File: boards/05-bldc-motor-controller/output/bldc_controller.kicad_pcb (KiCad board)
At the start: 2 copper layers, 80 x 100 mm, 55 parts, among them J1 Power Input, J2 Motor Output, J3 Hall Sensors, J4 SWD-6, Q1 IRLZ44N, Q2 IRLZ44N, Q3 IRLZ44N, Q4 IRLZ44N, Q5 IRLZ44N, Q6 IRLZ44N, U1 LM2596-5.0, U10 STM32G431K8Tx, U2 AMS1117-3.3, U3 DRV8301, Y1 8MHz

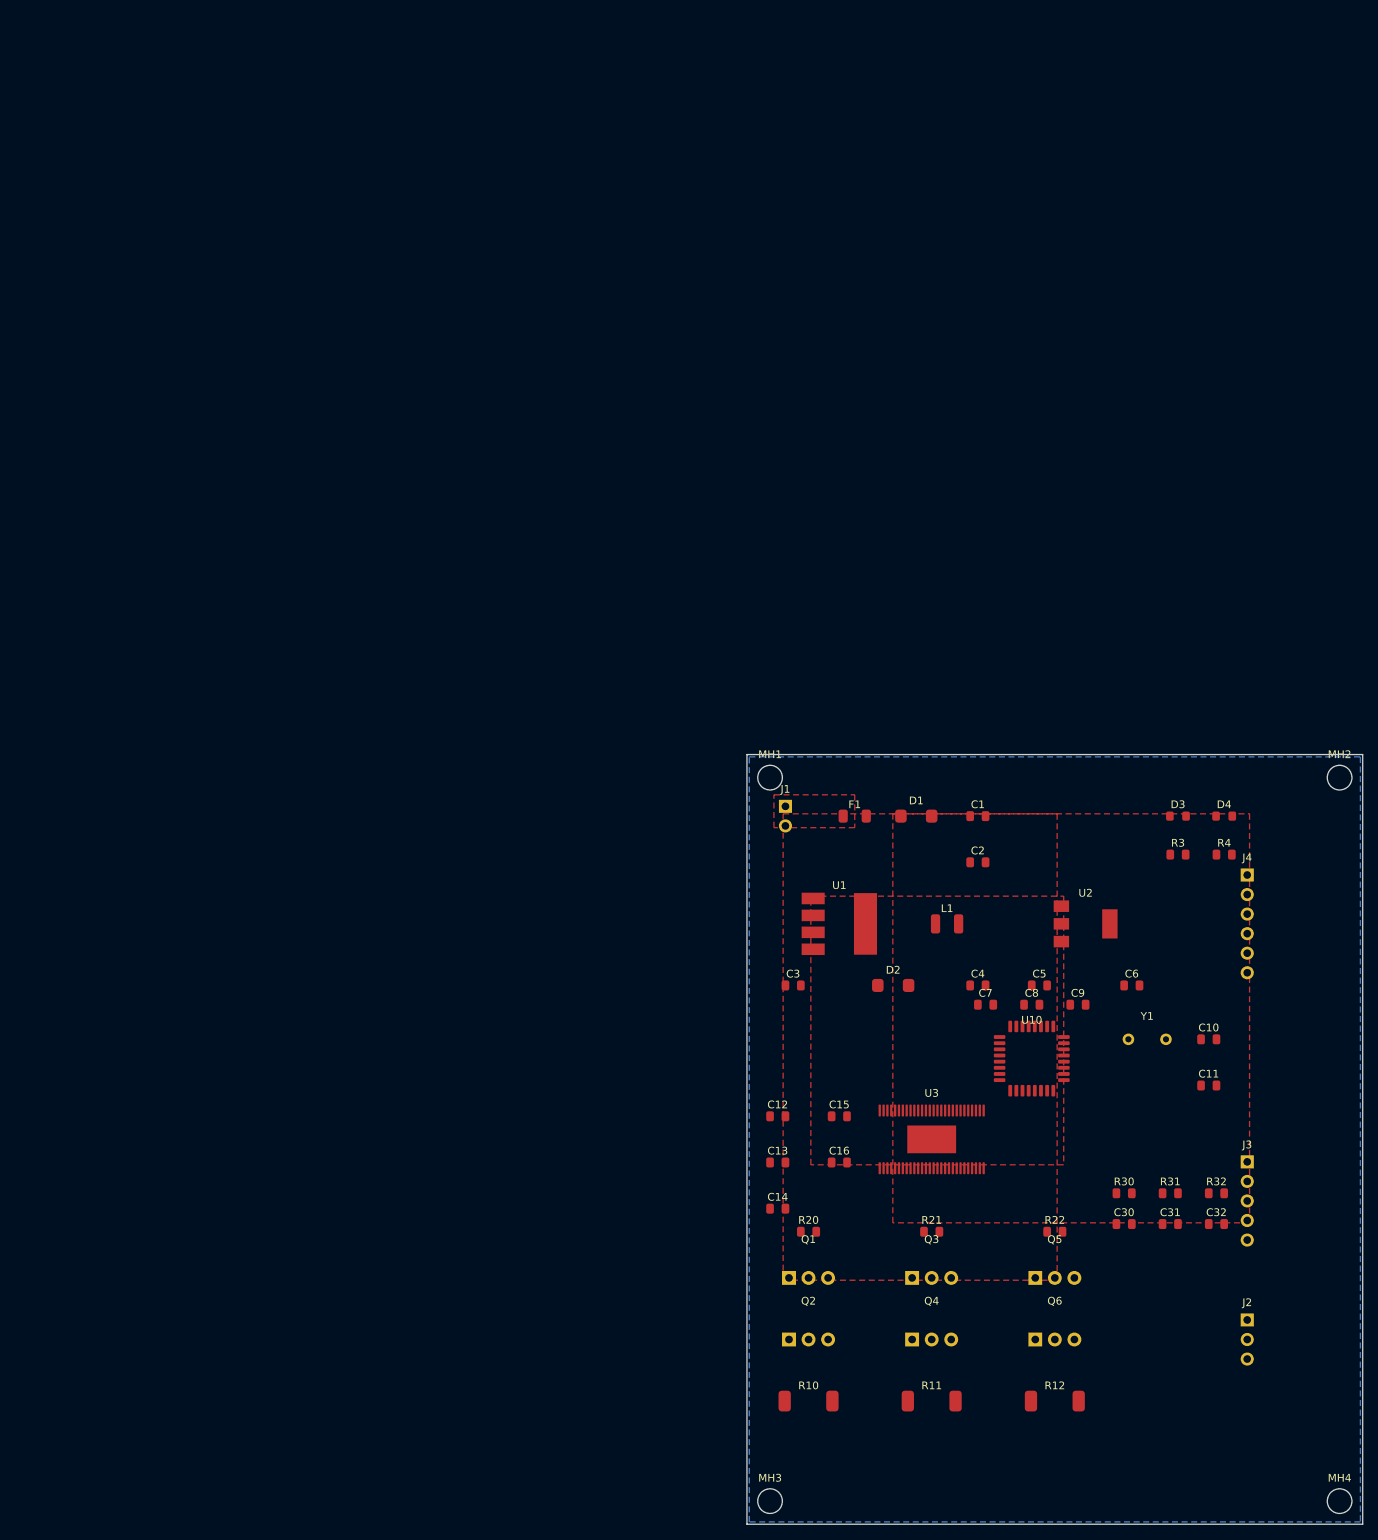
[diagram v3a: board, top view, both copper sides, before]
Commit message: feat(pcb): add page_fit to size sheet to board + center, apply to all boards
Add PCB.page_fit(margin=5.0) which rewrites the (paper ...) node to a tight
(paper "User" W H) sized to the Edge.Cuts bbox plus a uniform margin and
translates every board item (footprints, segments, vias, zones incl.
filled_polygons, gr_* graphics, text) so the board is centered with that
margin. Pure geometric translate — relative geometry, routing and DRC
validity are preserved, no re-route needed.

Expose it as `kct pcb page-fit <pcb> [-o out] [--margin] [--dry-run]` and
wire a PAGE_FIT build step (after stitch, before verify/export) so future
boards are centered too. Apply page_fit to all demo boards (00-07 +
external/softstart), both routed and unrouted PCBs, so the committed
layouts fill + center the KiCanvas viewer instead of sitting tiny in an A4
page. Boards 00/01 stay DRC-clean (0 errors); no board's DRC count changed.

Co-Authored-By: Claude Opus 4.7 <noreply@anthropic.com>
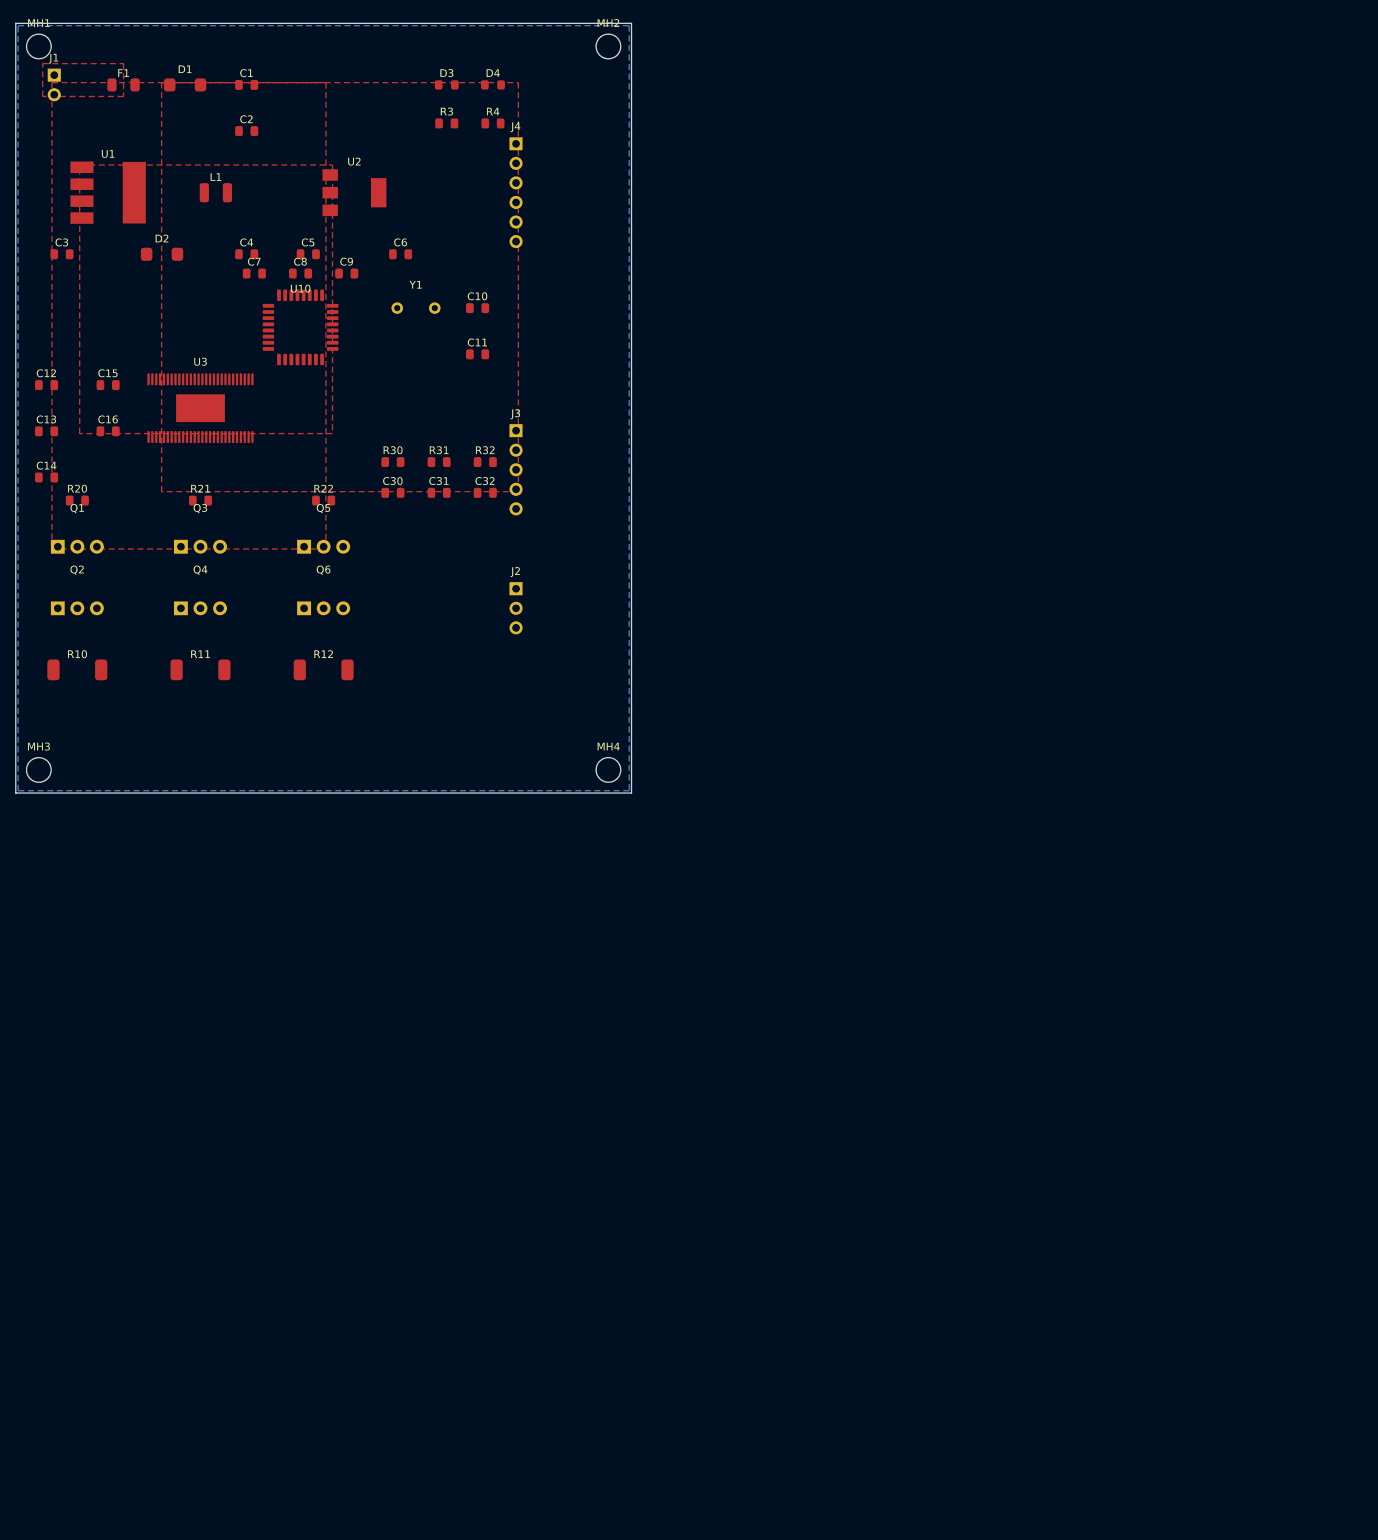
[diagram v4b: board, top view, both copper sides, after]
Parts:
- moved C1 134.4 mm to (35.0, 13.0)
- moved C10 134.4 mm to (65.0, 42.0)
- moved C11 134.4 mm to (65.0, 48.0)
- moved C12 134.4 mm to (9.00, 52.0)
- moved C13 134.4 mm to (9.00, 58.0)
- moved C14 134.4 mm to (9.00, 64.0)
- moved C15 134.4 mm to (17.0, 52.0)
- moved C16 134.4 mm to (17.0, 58.0)
- moved C2 134.4 mm to (35.0, 19.0)
- moved C3 134.4 mm to (11.0, 35.0)
- moved C30 134.4 mm to (54.0, 66.0)
- moved C31 134.4 mm to (60.0, 66.0)
- moved C32 134.4 mm to (66.0, 66.0)
- moved C4 134.4 mm to (35.0, 35.0)
- moved C5 134.4 mm to (43.0, 35.0)
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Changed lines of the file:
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@@
 (kicad_pcb
 	(version 20260206)
+	(paper "User" 90 110)
 	(generator "kicad-tools-demo")
 	(generator_version "10.0")
@@
 		(legacy_teardrops no)
 	)
-	(paper "A4")
 	(layers
 		(0 "F.Cu" signal)
@@
 	(net 52 "unconnected-(U10-PB5-Pad28)")
 	(gr_rect
-		(start 100.0 100.0)
-		(end 180.0 200.0)
+		(start 5 5)
+		(end 85 105)
 		(stroke
 			(width 0.1)
@@
 	(footprint "MountingHole:MountingHole_3.2mm_M3"
 		(layer "F.Cu")
-		(at 103.0 103.0)
+		(at 8 8)
 		(fp_text reference "MH1"
 			(at 0 -3)
@@
 	(footprint "MountingHole:MountingHole_3.2mm_M3"
 		(layer "F.Cu")
-		(at 177.0 103.0)
+		(at 82 8)
 		(fp_text reference "MH2"
 			(at 0 -3)
@@
 	(footprint "MountingHole:MountingHole_3.2mm_M3"
 		(layer "F.Cu")
-		(at 103.0 197.0)
+		(at 8 102)
 		(fp_text reference "MH3"
 			(at 0 -3)
@@
 	(footprint "MountingHole:MountingHole_3.2mm_M3"
 		(layer "F.Cu")
-		(at 177.0 197.0)
+		(at 82 102)
 		(fp_text reference "MH4"
 			(at 0 -3)
@@
 	(footprint "Connector_PinHeader_2.54mm:PinHeader_1x02_P2.54mm_Vertical"
 		(layer "F.Cu")
-		(at 105.0 108.0)
+		(at 10 13)
 		(fp_text reference "J1"
 			(at 0 -3.5)
@@
 	(footprint "Fuse:Fuse_1206_3216Metric"
 		(layer "F.Cu")
-		(at 114.0 108.0)
+		(at 19 13)
 		(fp_text reference "F1"
 			(at 0 -1.5)
@@
 	(footprint "Diode_SMD:D_SMA"
 		(layer "F.Cu")
-		(at 122.0 108.0)
+		(at 27 13)
 		(fp_text reference "D1"
 			(at 0 -2)
@@
 	(footprint "Capacitor_SMD:C_0805_2012Metric"
 		(layer "F.Cu")
-		(at 130.0 108.0)
+		(at 35 13)
 		(fp_text reference "C1"
 			(at 0 -1.5)
@@
 	(footprint "Capacitor_SMD:C_0805_2012Metric"
 		(layer "F.Cu")
-		(at 130.0 114.0)
+		(at 35 19)
 		(fp_text reference "C2"
 			(at 0 -1.5)
@@
 	(footprint "Package_TO_SOT_SMD:TO-263-5_TabPin3"
 		(layer "F.Cu")
-		(at 112.0 122.0)
+		(at 17 27)
 		(fp_text reference "U1"
 			(at 0 -5)
@@
 	(footprint "Inductor_SMD:L_1210_3225Metric"
 		(layer "F.Cu")
-		(at 126.0 122.0)
+		(at 31 27)
 		(fp_text reference "L1"
 			(at 0 -2)
@@
 	(footprint "Diode_SMD:D_SMA"
 		(layer "F.Cu")
-		(at 119.0 130.0)
+		(at 24 35)
 		(fp_text reference "D2"
 			(at 0 -2)
@@
 	(footprint "Capacitor_SMD:C_0805_2012Metric"
 		(layer "F.Cu")
-		(at 106.0 130.0)
+		(at 11 35)
 		(fp_text reference "C3"
 			(at 0 -1.5)
@@
 	(footprint "Capacitor_SMD:C_0805_2012Metric"
 		(layer "F.Cu")
-		(at 130.0 130.0)
+		(at 35 35)
 		(fp_text reference "C4"
 			(at 0 -1.5)
@@
 	(footprint "Package_TO_SOT_SMD:SOT-223-3_TabPin2"
 		(layer "F.Cu")
-		(at 144.0 122.0)
+		(at 49 27)
 		(fp_text reference "U2"
 			(at 0 -4)
@@
 	(footprint "Capacitor_SMD:C_0805_2012Metric"
 		(layer "F.Cu")
-		(at 138.0 130.0)
+		(at 43 35)
 		(fp_text reference "C5"
 			(at 0 -1.5)
@@
 	(footprint "Capacitor_SMD:C_0805_2012Metric"
 		(layer "F.Cu")
-		(at 150.0 130.0)
+		(at 55 35)
 		(fp_text reference "C6"
 			(at 0 -1.5)
@@
 	(footprint "Capacitor_SMD:C_0805_2012Metric"
 		(layer "F.Cu")
-		(at 131.0 132.5)
+		(at 36 37.5)
 		(fp_text reference "C7"
 			(at 0 -1.5)
@@
 	(footprint "Capacitor_SMD:C_0805_2012Metric"
 		(layer "F.Cu")
-		(at 137.0 132.5)
+		(at 42 37.5)
 		(fp_text reference "C8"
 			(at 0 -1.5)
@@
 	(footprint "Capacitor_SMD:C_0805_2012Metric"
 		(layer "F.Cu")
-		(at 143.0 132.5)
+		(at 48 37.5)
 		(fp_text reference "C9"
 			(at 0 -1.5)
@@
 	(footprint "Crystal:Crystal_HC49-4H_Vertical"
 		(layer "F.Cu")
-		(at 152.0 137.0)
+		(at 57 42)
 		(fp_text reference "Y1"
 			(at 0 -3)
@@
 	(footprint "Capacitor_SMD:C_0805_2012Metric"
 		(layer "F.Cu")
-		(at 160.0 137.0)
+		(at 65 42)
 		(fp_text reference "C10"
 			(at 0 -1.5)
@@
 	(footprint "Capacitor_SMD:C_0805_2012Metric"
 		(layer "F.Cu")
-		(at 160.0 143.0)
+		(at 65 48)
 		(fp_text reference "C11"
 			(at 0 -1.5)
@@
 	(footprint "Package_SO:HTSSOP-56-1EP_6.1x14mm_P0.5mm_EP3.61x6.35mm"
 		(layer "F.Cu")
-		(at 124.0 150.0)
+		(at 29 55)
 		(fp_text reference "U3"
 			(at 0 -6)
@@
 	(footprint "Capacitor_SMD:C_0805_2012Metric"
 		(layer "F.Cu")
-		(at 104.0 147.0)
+		(at 9 52)
 		(fp_text reference "C12"
 			(at 0 -1.5)
@@
 	(footprint "Capacitor_SMD:C_0805_2012Metric"
 		(layer "F.Cu")
-		(at 104.0 153.0)
+		(at 9 58)
 		(fp_text reference "C13"
 			(at 0 -1.5)
@@
 	(footprint "Capacitor_SMD:C_0805_2012Metric"
 		(layer "F.Cu")
-		(at 104.0 159.0)
+		(at 9 64)
 		(fp_text reference "C14"
 			(at 0 -1.5)
@@
 	(footprint "Capacitor_SMD:C_0805_2012Metric"
 		(layer "F.Cu")
-		(at 112.0 147.0)
+		(at 17 52)
 		(fp_text reference "C15"
 			(at 0 -1.5)
@@
 	(footprint "Capacitor_SMD:C_0805_2012Metric"
 		(layer "F.Cu")
-		(at 112.0 153.0)
+		(at 17 58)
 		(fp_text reference "C16"
 			(at 0 -1.5)
@@
 	(footprint "Package_QFP:LQFP-32_7x7mm_P0.8mm"
 		(layer "F.Cu")
-		(at 137.0 139.5)
+		(at 42 44.5)
 		(fp_text reference "U10"
 			(at 0 -5)
@@
 	(footprint "Package_TO_SOT_THT:TO-220-3_Vertical"
 		(layer "F.Cu")
-		(at 108.0 168.0)
+		(at 13 73)
 		(fp_text reference "Q1"
 			(at 0 -5)
@@
 	(footprint "Package_TO_SOT_THT:TO-220-3_Vertical"
 		(layer "F.Cu")
-		(at 108.0 176.0)
+		(at 13 81)
 		(fp_text reference "Q2"
 			(at 0 -5)
@@
 	(footprint "Package_TO_SOT_THT:TO-220-3_Vertical"
 		(layer "F.Cu")
-		(at 124.0 168.0)
+		(at 29 73)
 		(fp_text reference "Q3"
 			(at 0 -5)
@@
 	(footprint "Package_TO_SOT_THT:TO-220-3_Vertical"
 		(layer "F.Cu")
-		(at 124.0 176.0)
+		(at 29 81)
 		(fp_text reference "Q4"
 			(at 0 -5)
@@
 	(footprint "Package_TO_SOT_THT:TO-220-3_Vertical"
 		(layer "F.Cu")
-		(at 140.0 168.0)
+		(at 45 73)
 		(fp_text reference "Q5"
 			(at 0 -5)
@@
 	(footprint "Package_TO_SOT_THT:TO-220-3_Vertical"
 		(layer "F.Cu")
-		(at 140.0 176.0)
+		(at 45 81)
 		(fp_text reference "Q6"
 			(at 0 -5)
@@
 	(footprint "Resistor_SMD:R_2512_6332Metric"
 		(layer "F.Cu")
-		(at 108.0 184.0)
+		(at 13 89)
 		(fp_text reference "R10"
 			(at 0 -2)
@@
 	(footprint "Resistor_SMD:R_2512_6332Metric"
 		(layer "F.Cu")
-		(at 124.0 184.0)
+		(at 29 89)
 		(fp_text reference "R11"
 			(at 0 -2)
@@
 	(footprint "Resistor_SMD:R_2512_6332Metric"
 		(layer "F.Cu")
-		(at 140.0 184.0)
+		(at 45 89)
 		(fp_text reference "R12"
 			(at 0 -2)
@@
 	(footprint "Resistor_SMD:R_0805_2012Metric"
 		(layer "F.Cu")
-		(at 108.0 162.0)
+		(at 13 67)
 		(fp_text reference "R20"
 			(at 0 -1.5)
@@
 	(footprint "Resistor_SMD:R_0805_2012Metric"
 		(layer "F.Cu")
-		(at 124.0 162.0)
+		(at 29 67)
 		(fp_text reference "R21"
 			(at 0 -1.5)
@@
 	(footprint "Resistor_SMD:R_0805_2012Metric"
 		(layer "F.Cu")
-		(at 140.0 162.0)
+		(at 45 67)
 		(fp_text reference "R22"
 			(at 0 -1.5)
@@
 	(footprint "Connector_PinHeader_2.54mm:PinHeader_1x03_P2.54mm_Vertical"
 		(layer "F.Cu")
-		(at 165.0 176.0)
+		(at 70 81)
 		(fp_text reference "J2"
 			(at 0 -4.8)
@@
 	(footprint "Connector_PinHeader_2.54mm:PinHeader_1x05_P2.54mm_Vertical"
 		(layer "F.Cu")
-		(at 165.0 158.0)
+		(at 70 63)
 		(fp_text reference "J3"
 			(at 0 -7.3)
@@
 	(footprint "Connector_PinHeader_2.54mm:PinHeader_1x06_P2.54mm_Vertical"
 		(layer "F.Cu")
-		(at 165.0 122.0)
+		(at 70 27)
 		(fp_text reference "J4"
 			(at 0 -8.6)
@@
 	(footprint "Resistor_SMD:R_0805_2012Metric"
 		(layer "F.Cu")
-		(at 156.0 113.0)
+		(at 61 18)
 		(fp_text reference "R3"
 			(at 0 -1.5)
@@
 	(footprint "LED_SMD:LED_0805_2012Metric"
 		(layer "F.Cu")
-		(at 156.0 108.0)
+		(at 61 13)
 		(fp_text reference "D3"
 			(at 0 -1.5)
@@
 	(footprint "Resistor_SMD:R_0805_2012Metric"
 		(layer "F.Cu")
-		(at 162.0 113.0)
+		(at 67 18)
 		(fp_text reference "R4"
 			(at 0 -1.5)
@@
 	(footprint "LED_SMD:LED_0805_2012Metric"
 		(layer "F.Cu")
-		(at 162.0 108.0)
+		(at 67 13)
 		(fp_text reference "D4"
 			(at 0 -1.5)
@@
 	(footprint "Resistor_SMD:R_0805_2012Metric"
 		(layer "F.Cu")
-		(at 149.0 157.0)
+		(at 54 62)
 		(fp_text reference "R30"
 			(at 0 -1.5)
@@
 	(footprint "Resistor_SMD:R_0805_2012Metric"
 		(layer "F.Cu")
-		(at 155.0 157.0)
+		(at 60 62)
 		(fp_text reference "R31"
 			(at 0 -1.5)
@@
 	(footprint "Resistor_SMD:R_0805_2012Metric"
 		(layer "F.Cu")
-		(at 161.0 157.0)
+		(at 66 62)
 		(fp_text reference "R32"
 			(at 0 -1.5)
@@
 	(footprint "Capacitor_SMD:C_0805_2012Metric"
 		(layer "F.Cu")
-		(at 149.0 161.0)
+		(at 54 66)
 		(fp_text reference "C30"
 			(at 0 -1.5)
@@
 	(footprint "Capacitor_SMD:C_0805_2012Metric"
 		(layer "F.Cu")
-		(at 155.0 161.0)
+		(at 60 66)
 		(fp_text reference "C31"
 			(at 0 -1.5)
@@
 	(footprint "Capacitor_SMD:C_0805_2012Metric"
 		(layer "F.Cu")
-		(at 161.0 161.0)
+		(at 66 66)
 		(fp_text reference "C32"
 			(at 0 -1.5)
@@
 		(fill yes (thermal_gap 0.3) (thermal_bridge_width 0.4)
 		)
-		(polygon (pts (xy 100.3 100.3) (xy 179.7 100.3) (xy 179.7 199.7) (xy 100.3 199.7))
+		(polygon (pts (xy 5.3 5.3) (xy 84.7 5.3) (xy 84.7 104.7) (xy 5.3 104.7))
 		)
 	)
@@
 		(fill yes (thermal_gap 0.3) (thermal_bridge_width 0.4)
 		)
-		(polygon (pts (xy 104.7 107.7) (xy 140.3 107.7) (xy 140.3 168.3) (xy 104.7 168.3))
+		(polygon (pts (xy 9.7 12.7) (xy 45.3 12.7) (xy 45.3 73.3) (xy 9.7 73.3))
 		)
 	)
@@
 		(fill yes (thermal_gap 0.3) (thermal_bridge_width 0.4)
 		)
-		(polygon (pts (xy 108.3 118.4) (xy 141.15 118.4) (xy 141.15 153.3) (xy 108.3 153.3))
+		(polygon (pts (xy 13.3 23.4) (xy 46.15 23.4) (xy 46.15 58.3) (xy 13.3 58.3))
 		)
 	)
@@
 		(fill yes (thermal_gap 0.3) (thermal_bridge_width 0.4)
 		)
-		(polygon (pts (xy 118.95 107.7) (xy 165.3 107.7) (xy 165.3 160.84) (xy 118.95 160.84))
+		(polygon (pts (xy 23.95 12.7) (xy 70.3 12.7) (xy 70.3 65.84) (xy 23.95 65.84))
 		)
 	)
@@
 		(fill yes (thermal_gap 0.3) (thermal_bridge_width 0.4)
 		)
-		(polygon (pts (xy 103.5 105.23) (xy 114 105.23) (xy 114 109.5) (xy 103.5 109.5))
-		)
-	)
+		(polygon (pts (xy 8.5 10.23) (xy 19 10.23) (xy 19 14.5) (xy 8.5 14.5))
+		)
+	)
